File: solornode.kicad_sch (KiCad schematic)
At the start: 77 parts, among them J1 Conn_01x06, Q1 Q_NMOS_GDS, Q4 Q_PNP_BCE, Q5 Q_NPN_BCE, SW1 SW_Push, U1 LM358, U2 OC5864, U3 PY32F003F1xUx, U4 MAX485E, U5 SGM2033-5.0

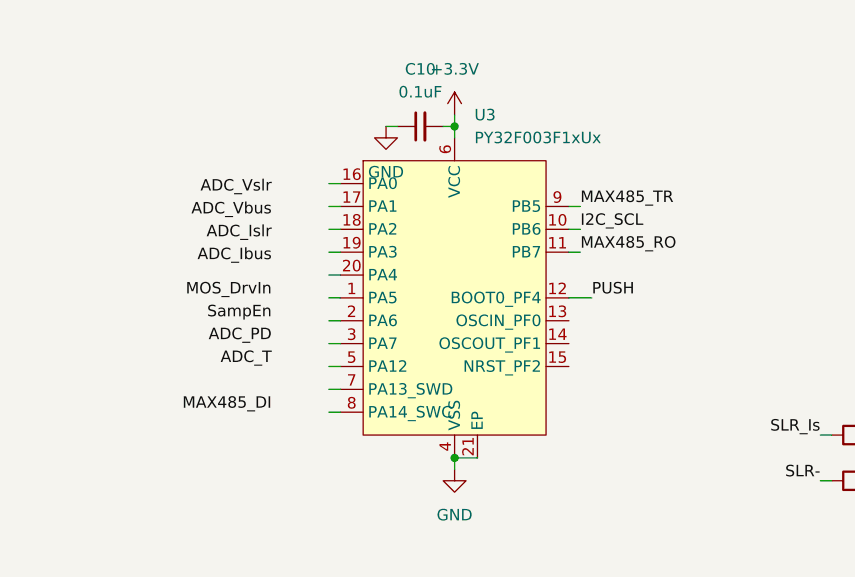
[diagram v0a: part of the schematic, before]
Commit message: 配置MCU引脚并连接
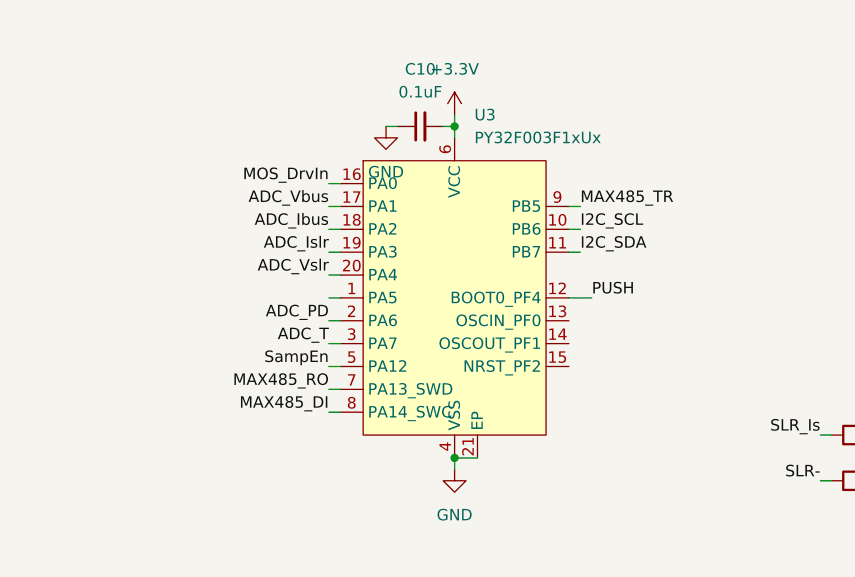
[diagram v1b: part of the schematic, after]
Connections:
- net ADC_Ibus: now also U3.18 (PA2)
- net ADC_Islr: now also U3.19 (PA3)
- net ADC_PD: now also U3.2 (PA6)
- net ADC_T: now also U3.3 (PA7)
- net ADC_Vbus: now also U3.17 (PA1)
- net ADC_Vslr: now also U3.20 (PA4)
- net MAX485_DI: now also U3.8 (PA14_SWC)
- net MAX485_RO: now also U3.7 (PA13_SWD); no longer U3.11 (PB7)
- net MOS_DrvIn: now also U3.16 (PA0)
- net SampEn: now also U3.5 (PA12)
- new net I2C_SDA: U3.11 (PB7)
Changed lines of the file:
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@@
-		)
-	)
-	(label "ADC_Ibus"
-		(at 162.56 101.6 180)
-		(effects
-			(font
-				(size 1.27 1.27)
-			)
-			(justify right bottom)
 		)
 	)
@@
 		)
 	)
+	(label "ADC_Ibus"
+		(at 168.91 97.79 180)
+		(effects
+			(font
+				(size 1.27 1.27)
+			)
+			(justify right bottom)
+		)
+	)
 	(label "MAX485_TR"
 		(at 196.85 95.25 0)
@@
 		)
 	)
-	(label "ADC_T"
-		(at 162.56 113.03 180)
-		(effects
-			(font
-				(size 1.27 1.27)
-			)
-			(justify right bottom)
-		)
-	)
 	(label "SLR+"
 		(at 27.94 24.13 0)
@@
 	)
 	(label "SampEn"
-		(at 162.56 107.95 180)
+		(at 168.91 113.03 180)
 		(effects
 			(font
@@
 		)
 	)
-	(label "MOS_DrvIn"
-		(at 162.56 105.41 180)
-		(effects
-			(font
-				(size 1.27 1.27)
-			)
-			(justify right bottom)
-		)
-	)
 	(label "PUSH"
 		(at 198.12 105.41 0)
@@
 		)
 	)
-	(label "ADC_PD"
-		(at 162.56 110.49 180)
-		(effects
-			(font
-				(size 1.27 1.27)
-			)
-			(justify right bottom)
-		)
-	)
 	(label "485-"
 		(at 27.94 36.83 0)
@@
 	)
 	(label "MOS_DrvIn"
+		(at 168.91 92.71 180)
+		(effects
+			(font
+				(size 1.27 1.27)
+			)
+			(justify right bottom)
+		)
+	)
+	(label "MOS_DrvIn"
 		(at 39.37 170.18 180)
 		(effects
@@
 		)
 	)
-	(label "ADC_Vslr"
-		(at 162.56 93.98 180)
-		(effects
-			(font
-				(size 1.27 1.27)
-			)
-			(justify right bottom)
-		)
-	)
-	(label "ADC_Vbus"
-		(at 162.56 96.52 180)
+	(label "ADC_Islr"
+		(at 168.91 100.33 180)
 		(effects
 			(font
@@
 		)
 	)
-	(label "MAX485_RO"
-		(at 196.85 100.33 0)
-		(effects
-			(font
-				(size 1.27 1.27)
-			)
-			(justify left bottom)
+	(label "ADC_Vslr"
+		(at 168.91 102.87 180)
+		(effects
+			(font
+				(size 1.27 1.27)
+			)
+			(justify right bottom)
 		)
 	)
@@
 		)
 	)
-	(label "ADC_Islr"
-		(at 162.56 99.06 180)
+	(label "ADC_Vbus"
+		(at 168.91 95.25 180)
+		(effects
+			(font
+				(size 1.27 1.27)
+			)
+			(justify right bottom)
+		)
+	)
+	(label "MAX485_RO"
+		(at 168.91 115.57 180)
 		(effects
 			(font
@@
 	)
 	(label "MAX485_DI"
-		(at 162.56 118.11 180)
+		(at 168.91 118.11 180)
+		(effects
+			(font
+				(size 1.27 1.27)
+			)
+			(justify right bottom)
+		)
+	)
+	(label "ADC_PD"
+		(at 168.91 107.95 180)
 		(effects
 			(font
@@
 		)
 	)
+	(label "I2C_SDA"
+		(at 196.85 100.33 0)
+		(effects
+			(font
+				(size 1.27 1.27)
+			)
+			(justify left bottom)
+		)
+	)
 	(label "SLR_Is"
 		(at 93.98 185.42 0)
@@
 		)
 	)
+	(label "ADC_T"
+		(at 168.91 110.49 180)
+		(effects
+			(font
+				(size 1.27 1.27)
+			)
+			(justify right bottom)
+		)
+	)

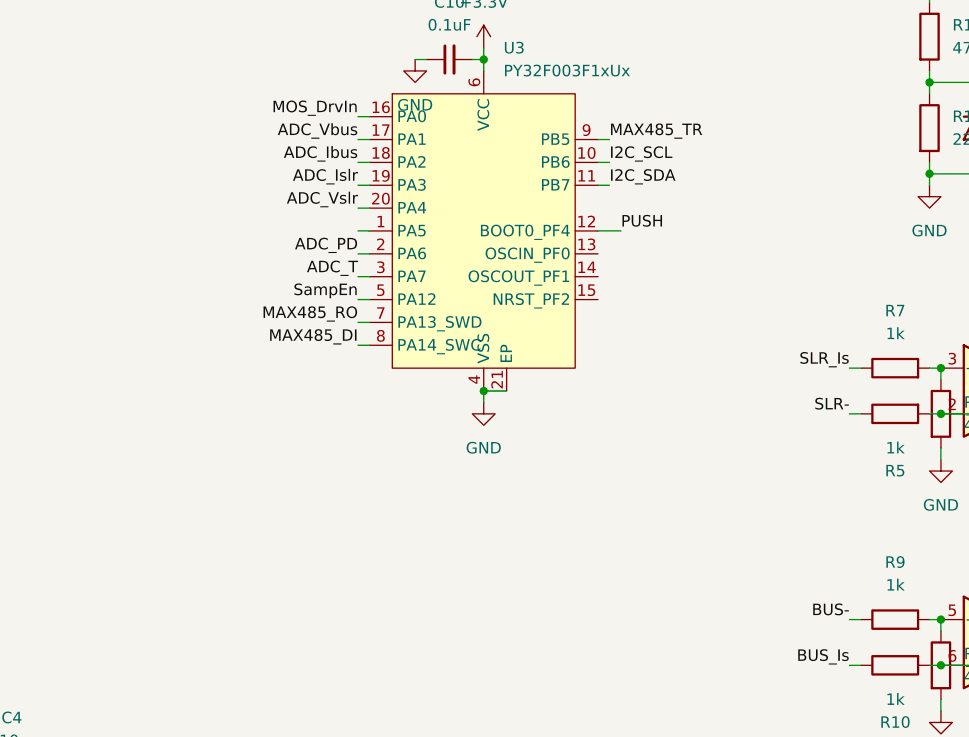
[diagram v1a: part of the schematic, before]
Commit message: 添加GPIO引出接口和一个LED
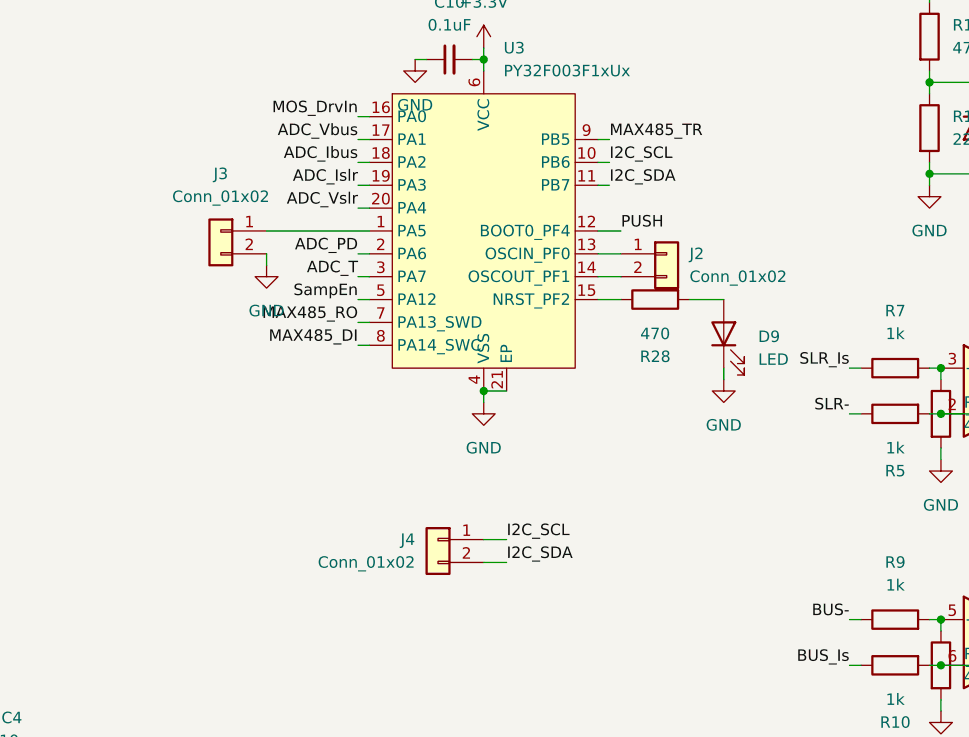
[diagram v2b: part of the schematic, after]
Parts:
- added D9: LED, LED_SMD:LED_0603_1608Metric, symbol Device:LED
- added J2, J3, J4: Conn_01x02, Resistor_SMD:R_0603_1608Metric, symbol Connector_Generic:Conn_01x02
- added R28: 470, Resistor_SMD:R_0402_1005Metric, symbol Device:R
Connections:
- net GND: now also D9.1 (K), J3.2 (Pin_2)
- net I2C_SCL: now also J4.1 (Pin_1)
- net I2C_SDA: now also J4.2 (Pin_2)
- net at U3.1 (PA5): now also J3.1 (Pin_1)
- net at U3.13 (OSCIN_PF0): now also J2.1 (Pin_1)
- net at U3.14 (OSCOUT_PF1): now also J2.2 (Pin_2)
- net at U3.15 (NRST_PF2): now also R28.1
- new net: D9.2 (A), R28.2

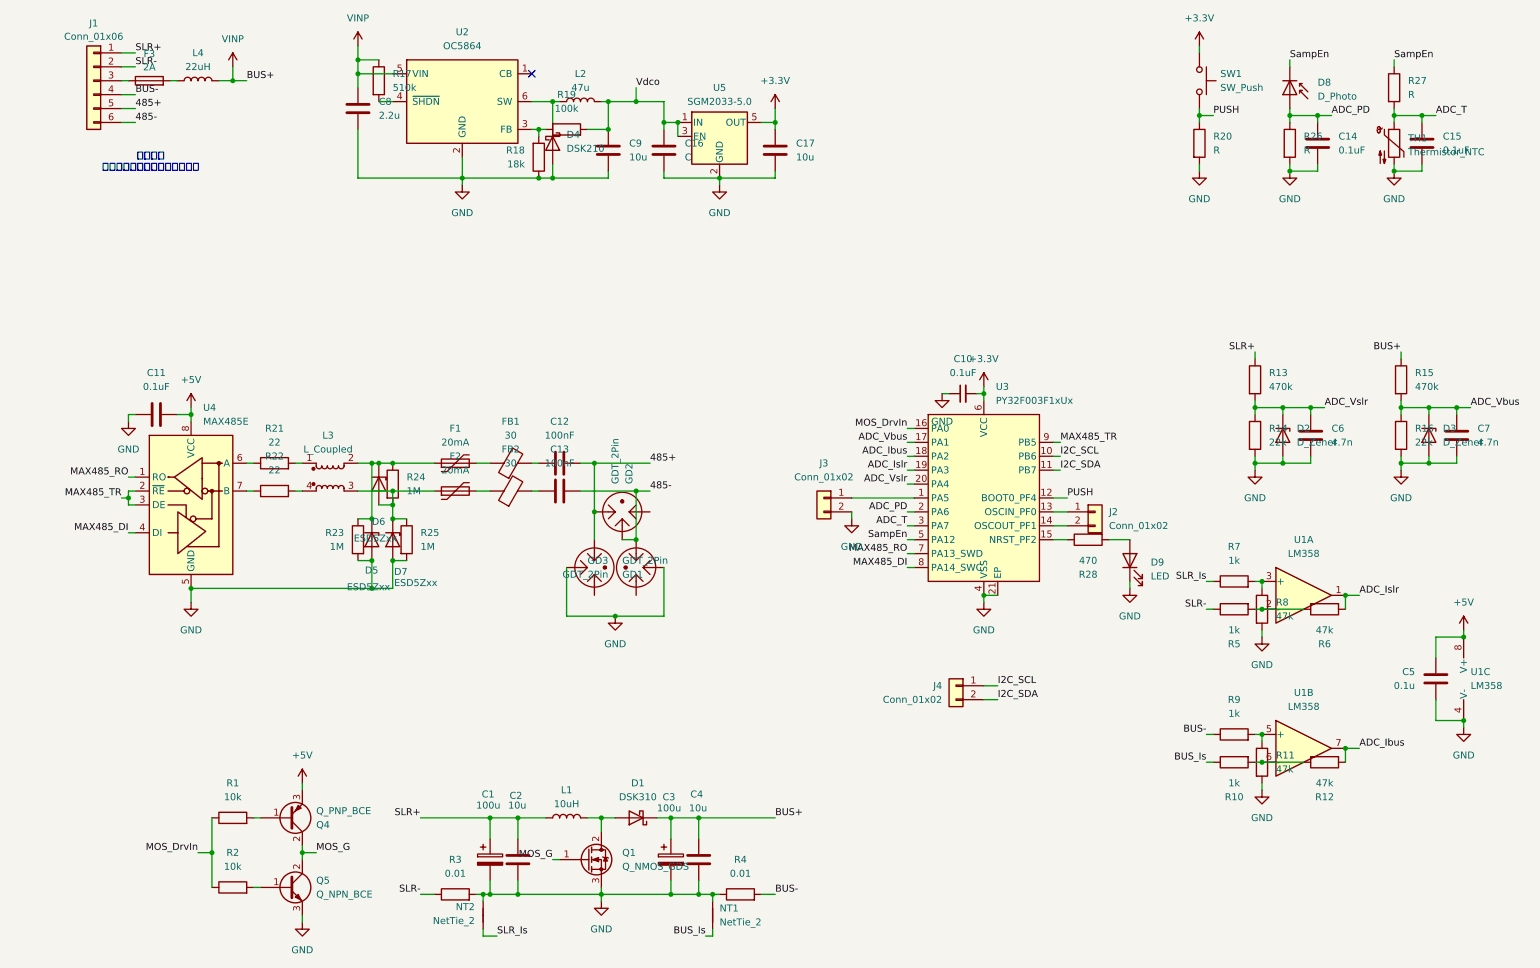
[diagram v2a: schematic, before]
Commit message: 添加稳压二极管进行电平转换，修改LDO为3.3V，连接5V线路
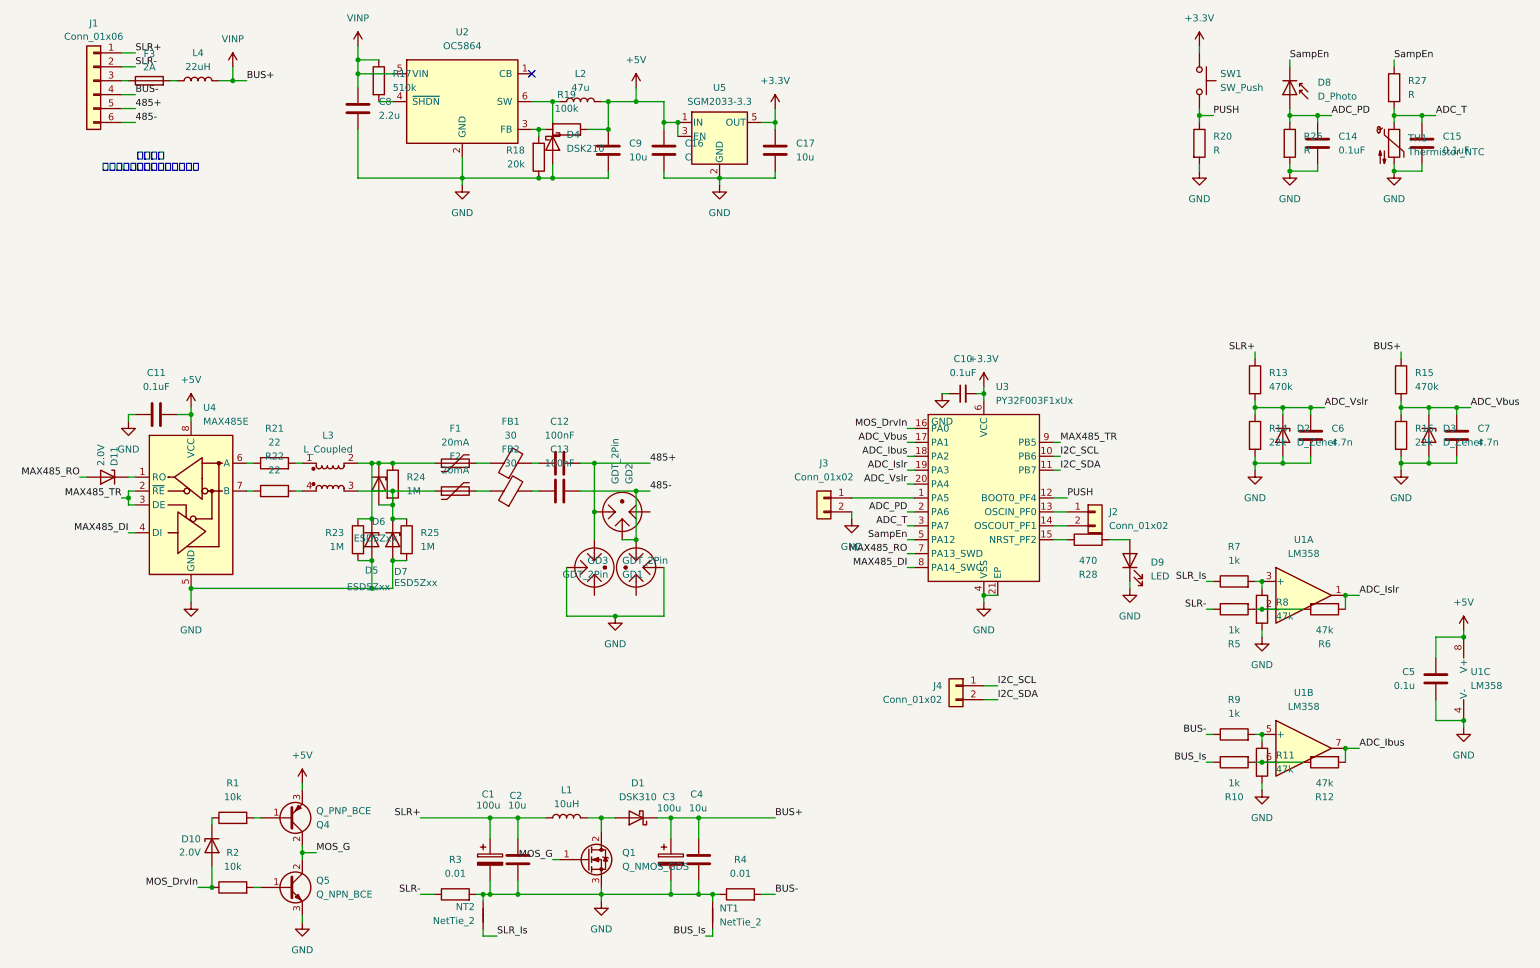
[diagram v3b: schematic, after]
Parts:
- added D10, D11: 2.0V, Diode_SMD:D_SOD-323, symbol Device:D_Zener
- R18: value 18k -> 20k
- U5: value SGM2033-5.0 -> SGM2033-3.3
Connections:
- net Vdco is gone; now on net +5V: C16.1, C9.1, L2.2, R19.2, U5.1 (IN), U5.3 (EN)
- net MAX485_RO: now also D11.2 (A); no longer U4.1 (RO)
- net MOS_DrvIn: now also D10.2 (A); no longer R1.1
- new net: D10.1 (K), R1.1
- new net: D11.1 (K), U4.1 (RO)
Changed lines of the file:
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@@
 	)
 	(junction
-		(at 41.91 170.18)
-		(diameter 0)
-		(color 0 0 0 0)
-	)
-	(junction
 		(at 222.25 35.56)
 		(diameter 0)
@@
 	)
 	(junction
+		(at 41.91 176.53)
+		(diameter 0)
+		(color 0 0 0 0)
+	)
+	(junction
 		(at 259.08 88.9)
 		(diameter 0)
@@
 	(wire
 		(pts
-			(xy 26.67 101.6) (xy 27.94 101.6)
+			(xy 17.78 101.6) (xy 19.05 101.6)
 		)
 		(stroke
@@
 	(wire
 		(pts
-			(xy 41.91 163.83) (xy 41.91 170.18)
-		)
-		(stroke
-			(width 0)
-			(type default)
-		)
-	)
-	(wire
-		(pts
 			(xy 262.89 35.56) (xy 265.43 35.56)
 		)
@@
 	(wire
 		(pts
+			(xy 41.91 172.72) (xy 41.91 176.53)
+		)
+		(stroke
+			(width 0)
+			(type default)
+		)
+	)
+	(wire
+		(pts
+			(xy 41.91 163.83) (xy 41.91 165.1)
+		)
+		(stroke
+			(width 0)
+			(type default)
+		)
+	)
+	(wire
+		(pts
 			(xy 158.75 107.95) (xy 158.75 109.22)
 		)
@@
 	(wire
 		(pts
+			(xy 26.67 101.6) (xy 27.94 101.6)
+		)
+		(stroke
+			(width 0)
+			(type default)
+		)
+	)
+	(wire
+		(pts
 			(xy 124.46 36.83) (xy 127 36.83)
 		)
@@
 	(wire
 		(pts
-			(xy 41.91 170.18) (xy 41.91 176.53)
-		)
-		(stroke
-			(width 0)
-			(type default)
-		)
-	)
-	(wire
-		(pts
 			(xy 168.91 118.11) (xy 170.18 118.11)
 		)
@@
 	(wire
 		(pts
-			(xy 39.37 170.18) (xy 41.91 170.18)
+			(xy 39.37 176.53) (xy 41.91 176.53)
 		)
 		(stroke
@@
 		)
 	)
-	(label "Vdco"
-		(at 119.38 30.48 0)
-		(effects
-			(font
-				(size 1.27 1.27)
-			)
-			(justify left bottom)
-		)
-	)
 	(label "ADC_Ibus"
 		(at 168.91 97.79 180)
@@
 	)
 	(label "MOS_DrvIn"
-		(at 39.37 170.18 180)
+		(at 39.37 176.53 180)
 		(effects
 			(font
@@
 	)
 	(label "MAX485_RO"
-		(at 26.67 101.6 180)
+		(at 17.78 101.6 180)
 		(effects
 			(font
@@
 			)
 		)
-		(property "Value" "SGM2033-5.0"
+		(property "Value" "SGM2033-3.3"
 			(at 134.62 33.02 0)
 			(effects
@@
 			)
 		)
-		(property "Value" "18k"
+		(property "Value" "20k"
 			(at 99.06 44.4499 0)
 			(effects
@@
 	)
 	(symbol
+		(lib_id "Device:D_Zener")
+		(at 22.86 101.6 0)
+		(mirror y)
+		(unit 1)
+		(exclude_from_sim no)
+		(in_bom yes)
+		(on_board yes)
+		(dnp no)
+		(property "Reference" "D11"
+			(at 24.0722 99.568 90)
+			(effects
+				(font
+					(size 1.27 1.27)
+				)
+				(justify left)
+			)
+		)
+		(property "Value" "2.0V"
+			(at 21.6479 99.568 90)
+			(effects
+				(font
+					(size 1.27 1.27)
+				)
+				(justify left)
+			)
+		)
+		(property "Footprint" "Diode_SMD:D_SOD-323"
+			(at 22.86 101.6 0)
+			(effects
+				(font
+					(size 1.27 1.27)
+				)
+				(hide yes)
+			)
+		)
+		(property "Datasheet" "~"
+			(at 22.86 101.6 0)
+			(effects
+				(font
+					(size 1.27 1.27)
+				)
+				(hide yes)
+			)
+		)
+		(property "Description" "Zener diode"
+			(at 22.86 101.6 0)
+			(effects
+				(font
+					(size 1.27 1.27)
+				)
+				(hide yes)
+			)
+		)
+		(pin "1"
+		)
+		(pin "2"
+		)
+		(instances
+			(project "solornode"
+				(path "/4bca4b2b-dcb0-465d-ab23-8d5d35a41dfe"
+					(reference "D11")
+					(unit 1)
+				)
+			)
+		)
+	)
+	(symbol
 		(lib_id "power:GND")
 		(at 134.62 48.26 0)
@@
 	)
 	(symbol
+		(lib_id "Device:D_Zener")
+		(at 41.91 168.91 90)
+		(mirror x)
+		(unit 1)
+		(exclude_from_sim no)
+		(in_bom yes)
+		(on_board yes)
+		(dnp no)
+		(property "Reference" "D10"
+			(at 39.878 167.6978 90)
+			(effects
+				(font
+					(size 1.27 1.27)
+				)
+				(justify left)
+			)
+		)
+		(property "Value" "2.0V"
+			(at 39.878 170.1221 90)
+			(effects
+				(font
+					(size 1.27 1.27)
+				)
+				(justify left)
+			)
+		)
+		(property "Footprint" "Diode_SMD:D_SOD-323"
+			(at 41.91 168.91 0)
+			(effects
+				(font
+					(size 1.27 1.27)
+				)
+				(hide yes)
+			)
+		)
+		(property "Datasheet" "~"
+			(at 41.91 168.91 0)
+			(effects
+				(font
+					(size 1.27 1.27)
+				)
+				(hide yes)
+			)
+		)
+		(property "Description" "Zener diode"
+			(at 41.91 168.91 0)
+			(effects
+				(font
+					(size 1.27 1.27)
+				)
+				(hide yes)
+			)
+		)
+		(pin "1"
+		)
+		(pin "2"
+		)
+		(instances
+			(project ""
+				(path "/4bca4b2b-dcb0-465d-ab23-8d5d35a41dfe"
+					(reference "D10")
+					(unit 1)
+				)
+			)
+		)
+	)
+	(symbol
 		(lib_id "Device:C")
 		(at 97.79 171.45 0)
@@
 					(unit 1)
 				)
+			)
+		)
+	)
+	(symbol
+		(lib_id "power:+5V")
+		(at 119.38 30.48 0)
+		(unit 1)
+		(exclude_from_sim no)
+		(in_bom yes)
+		(on_board yes)
+		(dnp no)
+		(fields_autoplaced yes)
+		(property "Reference" "#PWR28"
+			(at 119.38 34.29 0)
+			(effects
+				(font
+					(size 1.27 1.27)
+				)
+				(hide yes)
+			)
+		)
+		(property "Value" "+5V"
+			(at 119.38 25.4 0)
+			(effects
+				(font
+					(size 1.27 1.27)
+				)
+			)
+		)
+		(property "Footprint" ""
+			(at 119.38 30.48 0)
+			(effects
+				(font
+					(size 1.27 1.27)
+				)
+				(hide yes)
+			)
+		)
+		(property "Datasheet" ""
+			(at 119.38 30.48 0)
+			(effects
+				(font
+					(size 1.27 1.27)
+				)
+				(hide yes)
+			)
+		)
+		(property "Description" "Power symbol creates a global label with name \"+5V\""
+			(at 119.38 30.48 0)
+			(effects
+				(font
+					(size 1.27 1.27)
+				)
+				(hide yes)
+			)
+		)
+		(pin "1"
+		)
+		(instances
+			(project "solornode"
+				(path "/4bca4b2b-dcb0-465d-ab23-8d5d35a41dfe"
+					(reference "#PWR28")
+					(unit 1)
+				)
